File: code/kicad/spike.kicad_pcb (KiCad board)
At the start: 2 copper layers, 80 x 50 mm, 4 parts, among them J1A ESP32-C3-SuperMini-L, J1B ESP32-C3-SuperMini-R, J2 SCD41_Breakout, J3 BH1750_GY302

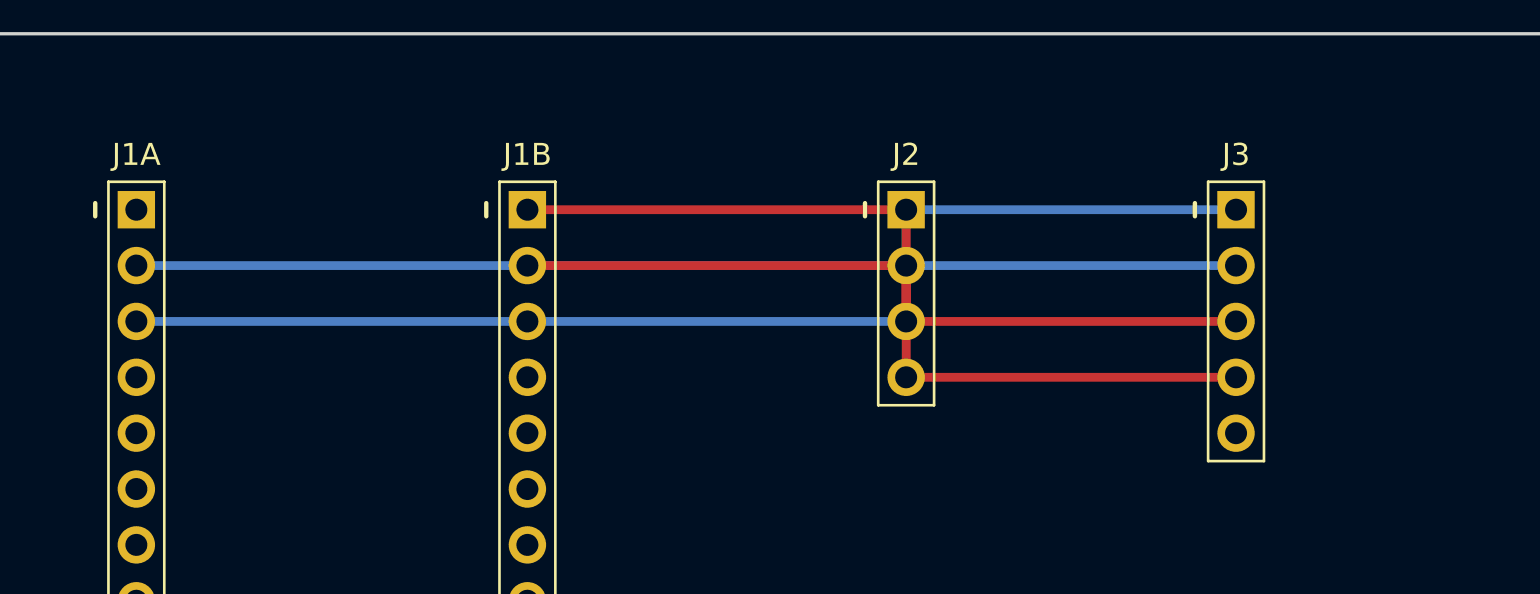
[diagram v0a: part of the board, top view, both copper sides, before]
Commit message: chore(kicad): regenerate spike.kicad_pcb with rotated sensors
The generator in PR #26 added the rotation logic but the checked-in
spike.kicad_pcb was still the pre-rotation output. Regenerate to
match — J2 and J3 now carry (at … 270.0) and the routing pad
coordinates reflect the rotated headers.

Co-Authored-By: Claude Opus 4.7 (1M context) <noreply@anthropic.com>
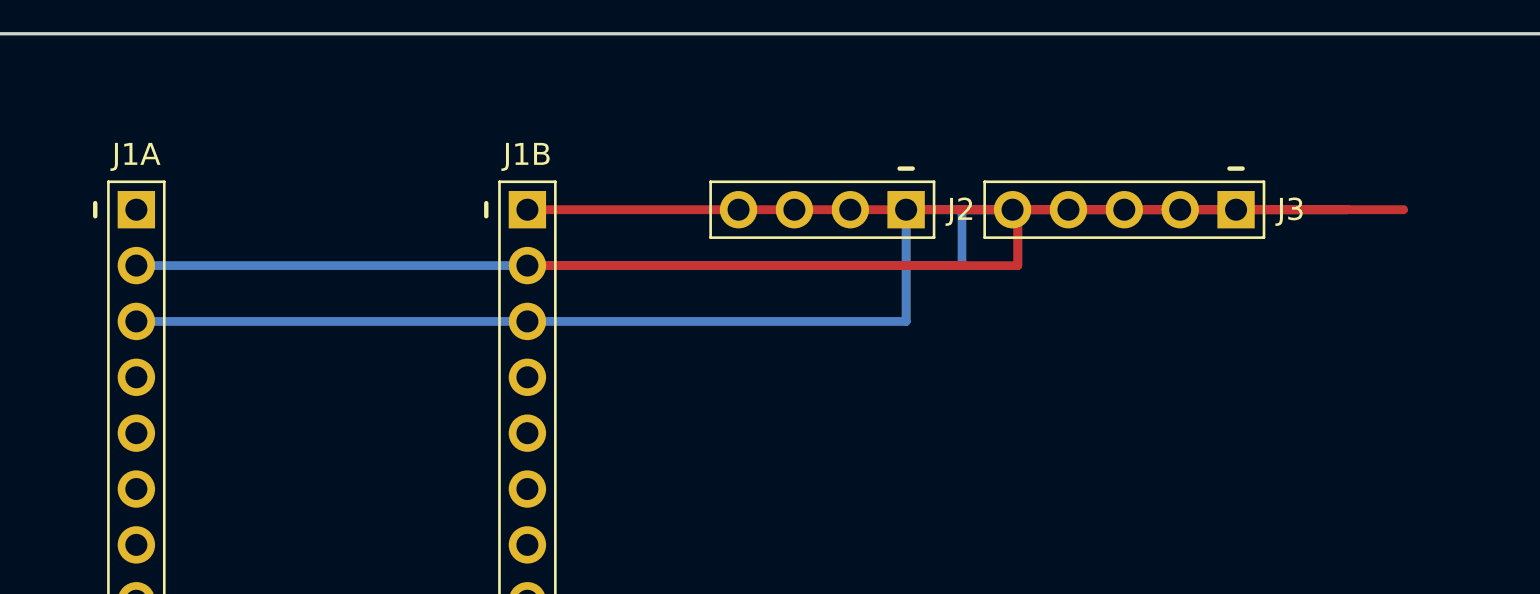
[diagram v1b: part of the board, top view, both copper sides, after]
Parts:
- turned J2 to 270 degrees
- turned J3 to 270 degrees
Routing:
- net SCL: track 34.8 -> 39.8 mm
- net GND: track 50.0 -> 55.1 mm
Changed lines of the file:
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@@
 	(footprint "spike:PinHeader_1x04"
 		(layer "F.Cu")
-		(at 145.0 68.0)
+		(at 145.0 68.0 270.0)
 		(descr "Sensirion SCD41 breakout 1x4 female header")
 		(tags "pin header through-hole")
@@
 	(footprint "spike:PinHeader_1x05"
 		(layer "F.Cu")
-		(at 160.0 68.0)
+		(at 160.0 68.0 270.0)
 		(descr "Rohm BH1750 GY-302 breakout 1x5 female header")
 		(tags "pin header through-hole")
@@
 	(segment
 		(start 127.78 68.0)
-		(end 145.0 68.0)
-		(width 0.4)
-		(layer "F.Cu")
-		(net 3)
-	)
-	(segment
-		(start 145.0 68.0)
-		(end 145.0 75.62)
-		(width 0.4)
-		(layer "F.Cu")
-		(net 3)
-	)
-	(segment
-		(start 145.0 75.62)
-		(end 160.0 75.62)
-		(width 0.4)
-		(layer "F.Cu")
-		(net 3)
-	)
-	(segment
-		(start 160.0 75.62)
-		(end 160.0 75.62)
+		(end 152.62 68.0)
+		(width 0.4)
+		(layer "F.Cu")
+		(net 3)
+	)
+	(segment
+		(start 152.62 68.0)
+		(end 152.62 68.0)
+		(width 0.4)
+		(layer "F.Cu")
+		(net 3)
+	)
+	(segment
+		(start 152.62 68.0)
+		(end 167.62 68.0)
+		(width 0.4)
+		(layer "F.Cu")
+		(net 3)
+	)
+	(segment
+		(start 167.62 68.0)
+		(end 167.62 68.0)
 		(width 0.4)
 		(layer "F.Cu")
@@
 	(segment
 		(start 127.78 70.54)
-		(end 145.0 70.54)
-		(width 0.4)
-		(layer "F.Cu")
-		(net 4)
-	)
-	(segment
-		(start 145.0 70.54)
-		(end 145.0 73.08)
-		(width 0.4)
-		(layer "F.Cu")
-		(net 4)
-	)
-	(segment
-		(start 145.0 73.08)
-		(end 160.0 73.08)
-		(width 0.4)
-		(layer "F.Cu")
-		(net 4)
-	)
-	(segment
-		(start 160.0 73.08)
-		(end 160.0 73.08)
+		(end 150.08 70.54)
+		(width 0.4)
+		(layer "F.Cu")
+		(net 4)
+	)
+	(segment
+		(start 150.08 70.54)
+		(end 150.08 68.0)
+		(width 0.4)
+		(layer "F.Cu")
+		(net 4)
+	)
+	(segment
+		(start 150.08 68.0)
+		(end 165.08 68.0)
+		(width 0.4)
+		(layer "F.Cu")
+		(net 4)
+	)
+	(segment
+		(start 165.08 68.0)
+		(end 165.08 68.0)
 		(width 0.4)
 		(layer "F.Cu")
@@
 	(segment
 		(start 110.0 70.54)
-		(end 145.0 70.54)
+		(end 147.54 70.54)
 		(width 0.4)
 		(layer "B.Cu")
@@
 	)
 	(segment
-		(start 145.0 70.54)
-		(end 145.0 70.54)
+		(start 147.54 70.54)
+		(end 147.54 68.0)
 		(width 0.4)
 		(layer "B.Cu")
@@
 	)
 	(segment
-		(start 145.0 70.54)
-		(end 160.0 70.54)
+		(start 147.54 68.0)
+		(end 162.54 68.0)
 		(width 0.4)
 		(layer "B.Cu")
@@
 	)
 	(segment
-		(start 160.0 70.54)
-		(end 160.0 70.54)
-		(width 0.4)
-		(layer "B.Cu")
+		(start 162.54 68.0)
+		(end 162.54 68.0)
+		(width 0.4)
+		(layer "B.Cu")
